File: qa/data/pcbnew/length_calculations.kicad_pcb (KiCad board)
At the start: 2 copper layers, 21.8 x 34 mm, 12 parts

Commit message: Use full start / end copper layer heights in length calculations
Previously we halved the start / end copper layer heights, which is
not in line with how other EDA tools behave. This was also inconsistent
with adding pad-to-die lengths as we did not add back in the missing
half.

Fixes https://gitlab.com/kicad/code/kicad/-/issues/21365
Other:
- board text added: "Single track from pad to pad, with pad in via. Length 14.9150mm (13.3350mm track, 1.5800mm via)"
- board text added: "Track from pad to pad with two vias in track. Length 16.4950mm (13.3350mm track, 3.1600mm via)"
- board text added: "Track from pad to pad with via in track. Length 14.9150mm (13.3350mm track, 1.5800mm via)"
- board text removed: "Single track from pad to pad, with pad in via. Length 14.880mm (13.3350mm track, 1.545mm via)"
- board text removed: "Track from pad to pad with two vias in track. Length 16.4250mm (13.3350mm track, 3.0900mm via)"
- board text removed: "Track from pad to pad with via in track. Length 14.880mm (13.3350mm track, 1.545mm via)"
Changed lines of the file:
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@@
 (kicad_pcb
-	(version 20250324)
+	(version 20250801)
 	(generator "pcbnew")
 	(generator_version "9.99")
@@
 			(usegerberadvancedattributes yes)
 			(creategerberjobfile yes)
-			(dashed_line_dash_ratio 12.000000)
-			(dashed_line_gap_ratio 3.000000)
+			(dashed_line_dash_ratio 12)
+			(dashed_line_gap_ratio 3)
 			(svgprecision 4)
 			(plotframeref no)
 			(mode 1)
 			(useauxorigin no)
-			(hpglpennumber 1)
-			(hpglpenspeed 20)
-			(hpglpendiameter 15.000000)
 			(pdf_front_fp_property_popups yes)
 			(pdf_back_fp_property_popups yes)
@@
 		)
 	)
-	(gr_text "Single track from pad to pad, with pad in via.\nLength 14.880mm (13.3350mm track, 1.545mm via)"
+	(gr_text "Single track from pad to pad, with pad in via.\nLength 14.9150mm (13.3350mm track, 1.5800mm via)"
 		(at 140.335 55.118 0)
 		(layer "User.1")
@@
 		)
 	)
-	(gr_text "Track from pad to pad with two vias in track.\nLength 16.4250mm (13.3350mm track, 3.0900mm via)"
+	(gr_text "Track from pad to pad with two vias in track.\nLength 16.4950mm (13.3350mm track, 3.1600mm via)"
 		(at 140.335 66.04 0)
 		(layer "User.1")
@@
 		)
 	)
-	(gr_text "Track from pad to pad with via in track.\nLength 14.880mm (13.3350mm track, 1.545mm via)"
+	(gr_text "Track from pad to pad with via in track.\nLength 14.9150mm (13.3350mm track, 1.5800mm via)"
 		(at 140.335 60.706 0)
 		(layer "User.1")

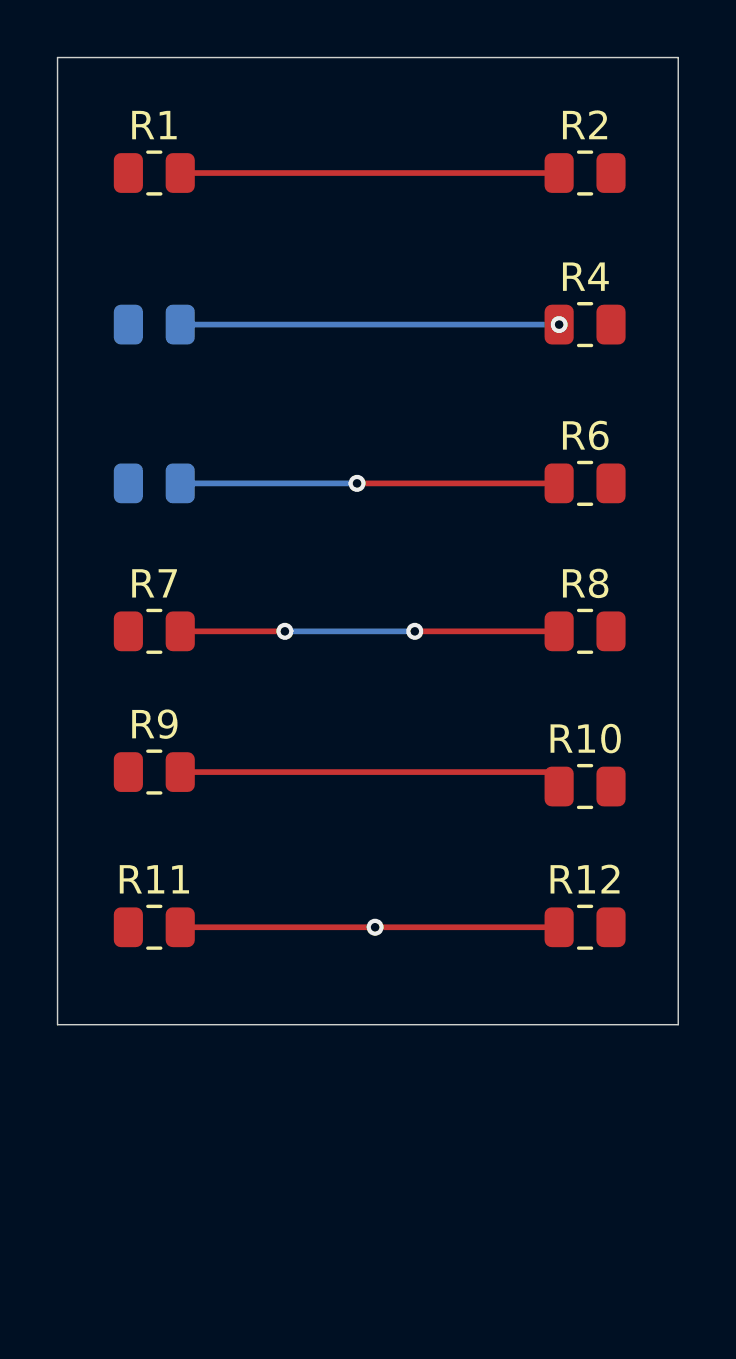
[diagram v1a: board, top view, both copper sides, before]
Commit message: Improve via height electrial length calculations
For vias which terminate electrically in an internal layer, only
count half of that internal layer height. This means a subsequent
via on the same route will not result on the internal layer being
double-counted.

Fixes https://gitlab.com/kicad/code/kicad/-/work_items/24118
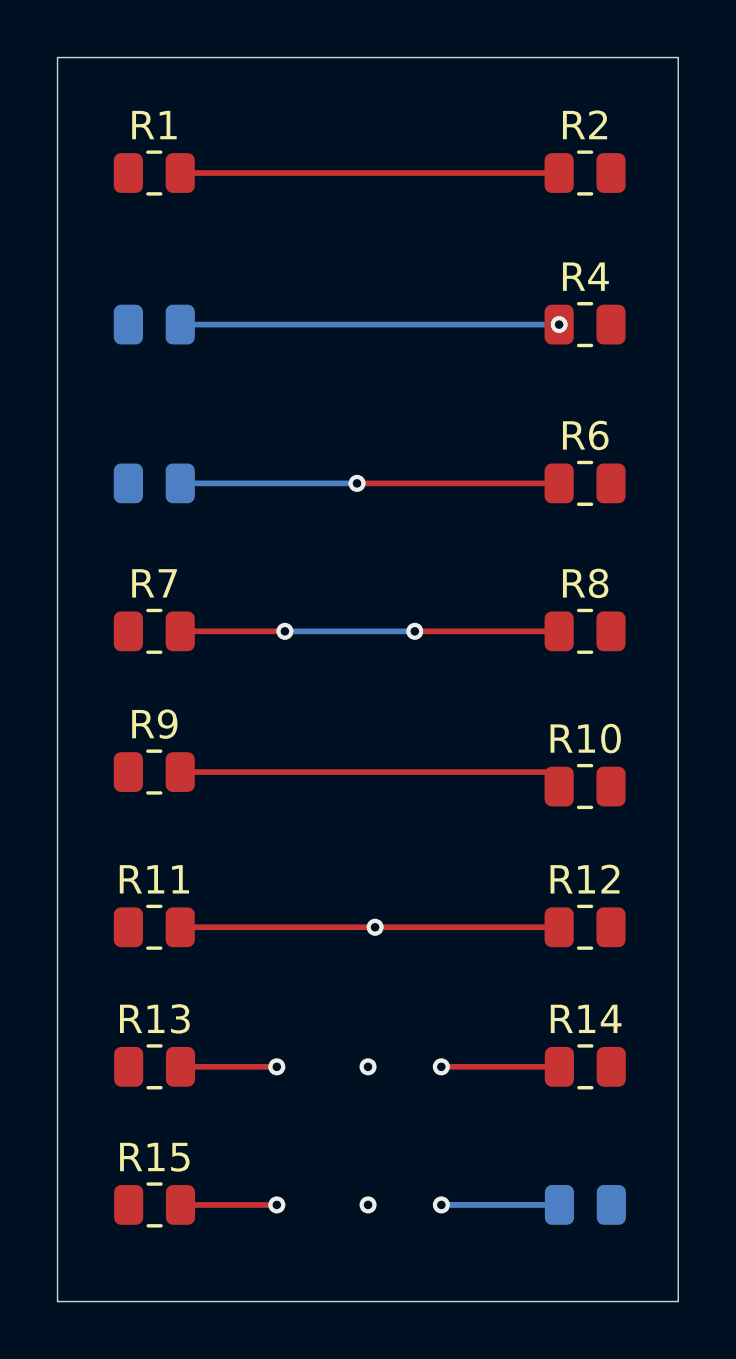
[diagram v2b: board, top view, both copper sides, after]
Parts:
- added R13: R, Resistor_SMD:R_0805_2012Metric, F.Cu at (121.4, 80.3)
- added R14: R, Resistor_SMD:R_0805_2012Metric, F.Cu at (136.6, 80.3)
- added R15: R, Resistor_SMD:R_0805_2012Metric, F.Cu at (121.4, 85.2)
- added R16: R, Resistor_SMD:R_0805_2012Metric, B.Cu at (136.6, 85.2)
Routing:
- net Net-(R15-Pad2): track 0.00 -> 13.3 mm, vias 0 -> 3
- net Net-(R13-Pad2): track 0.00 -> 13.3 mm, vias 0 -> 3
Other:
- board size 21.8 x 34 mm -> 21.8 x 43.8 mm
- copper layers 2 -> 4
- board text added: "Single track from pad to pad through internal layer vias. Length 13.3350mm (13.3350mm track, 20.1750mm via)"
- board text added: "Single track from pad to pad through internal layer vias. Length 28.4750mm (13.3350mm track, 15.1400mm via)"
- board text added: "Single track from pad to pad, with pad in via. Length 28.4750mm (13.3350mm track, 15.1400mm via)"
- board text added: "Track from pad to pad with two vias in track. Length 43.6150mm (13.3350mm track, 30.2800mm via)"
- board text added: "Track from pad to pad with via in track. Length 28.4750mm (13.3350mm track, 15.1400mm via)"
- board text removed: "Single track from pad to pad, with pad in via. Length 14.9150mm (13.3350mm track, 1.5800mm via)"
- board text removed: "Track from pad to pad with two vias in track. Length 16.4950mm (13.3350mm track, 3.1600mm via)"
- board text removed: "Track from pad to pad with via in track. Length 14.9150mm (13.3350mm track, 1.5800mm via)"
